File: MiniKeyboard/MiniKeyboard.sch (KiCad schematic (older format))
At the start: 50 parts

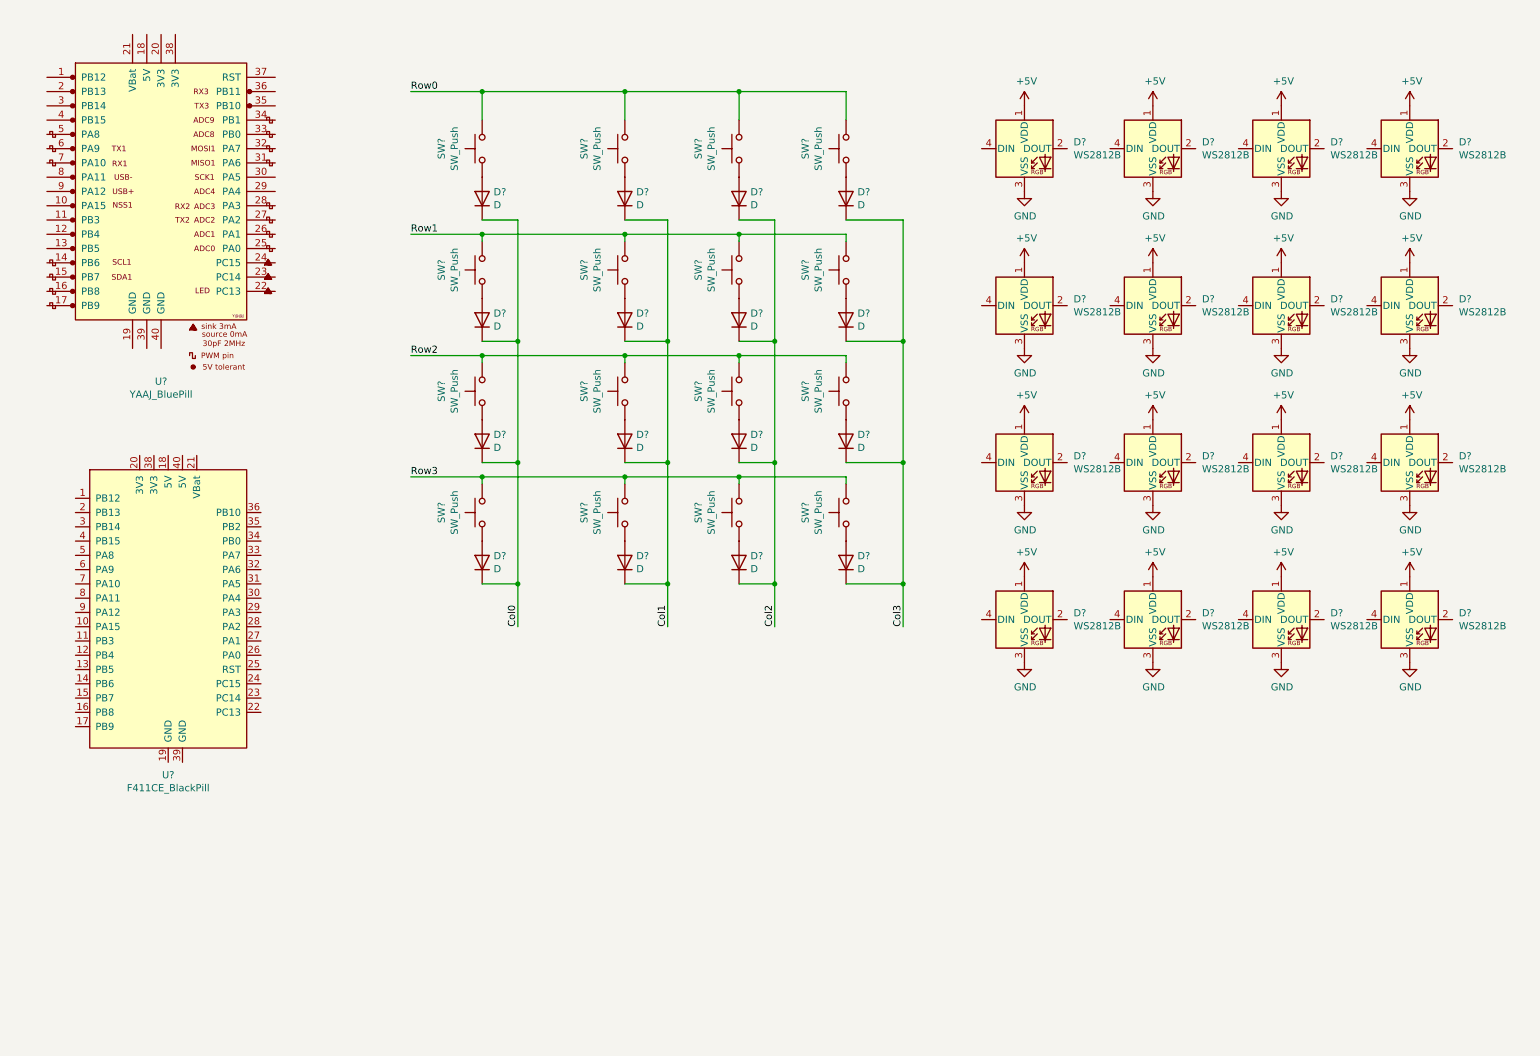
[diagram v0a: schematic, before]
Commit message: Added 411CE Blackpill to minikeyboard
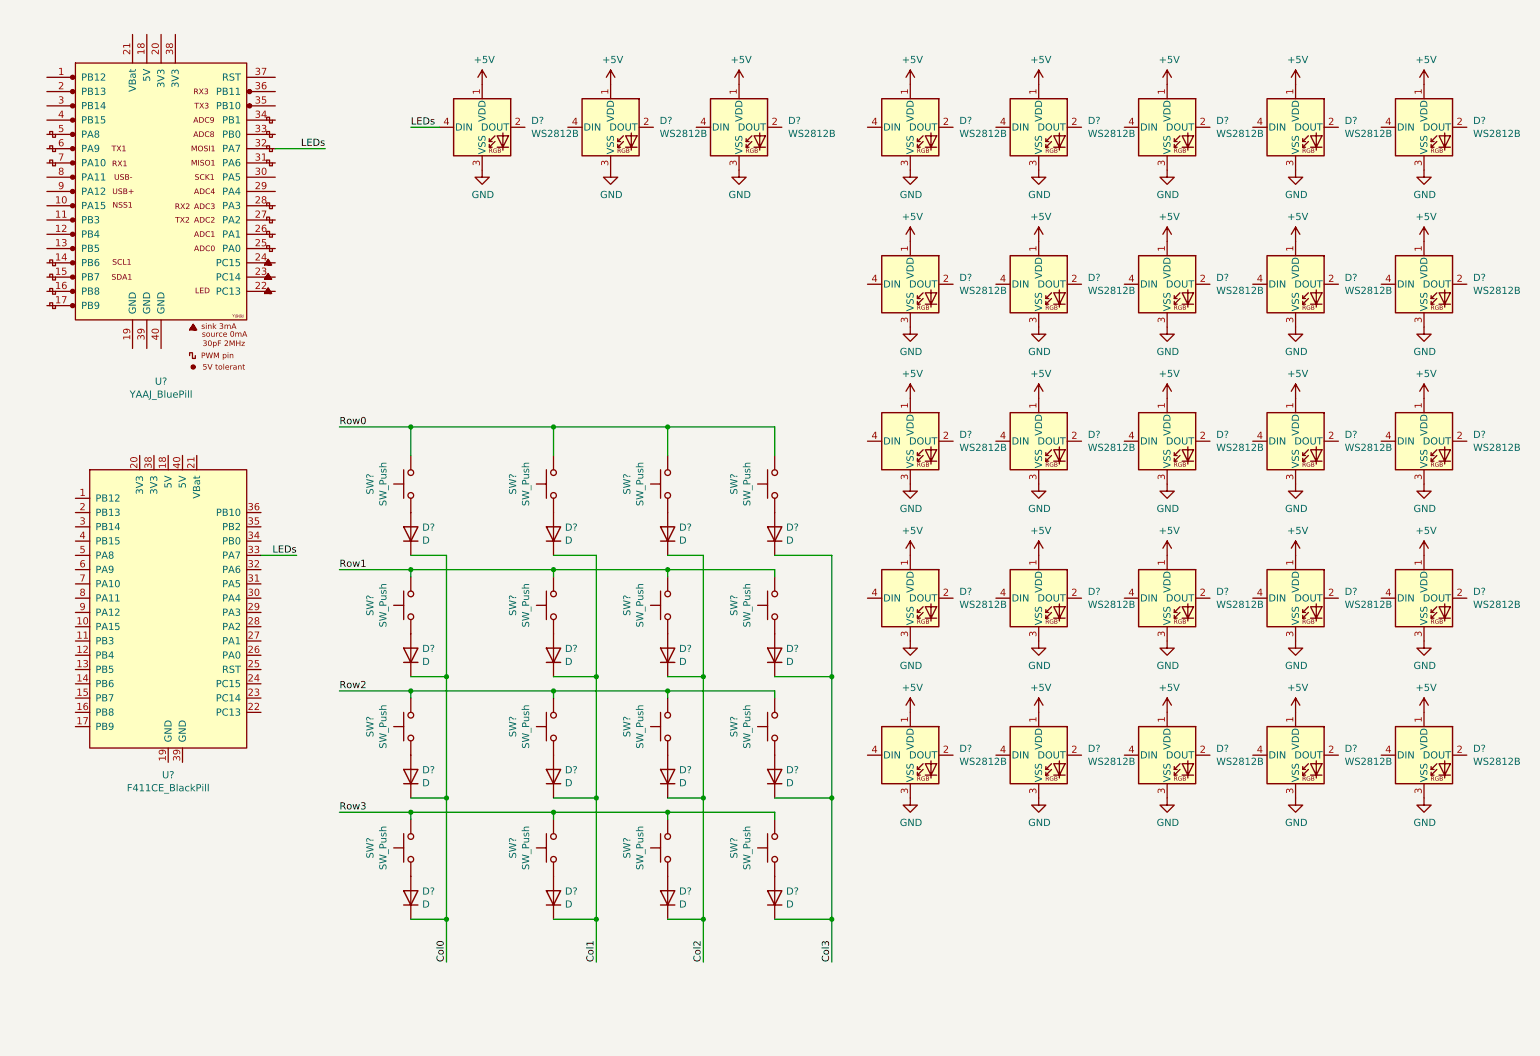
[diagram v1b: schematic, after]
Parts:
- added D? (x12): WS2812B, LED_SMD:LED_WS2812B_PLCC4_5.0x5.0mm_P3.2mm, symbol LED:WS2812B
- U?: footprint (none) -> MiniKeyboard:F411CE-Blackpill
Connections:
- net +5V: now also D?.1 (VDD), D?.1 (VDD), D?.1 (VDD), D?.1 (VDD), D?.1 (VDD), D?.1 (VDD), D?.1 (VDD), D?.1 (VDD), D?.1 (VDD), D?.1 (VDD), D?.1 (VDD), D?.1 (VDD)
- net GND: now also D?.3 (VSS), D?.3 (VSS), D?.3 (VSS), D?.3 (VSS), D?.3 (VSS), D?.3 (VSS), D?.3 (VSS), D?.3 (VSS), D?.3 (VSS), D?.3 (VSS), D?.3 (VSS), D?.3 (VSS)
- net LEDs: now reaches U?.33 (PA7)
- net LEDs: now also U?.32 (PA7), D?.4 (DIN)
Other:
- moved on the sheet: D?, SW?

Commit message: fixed minikeyboard after moving libraries around
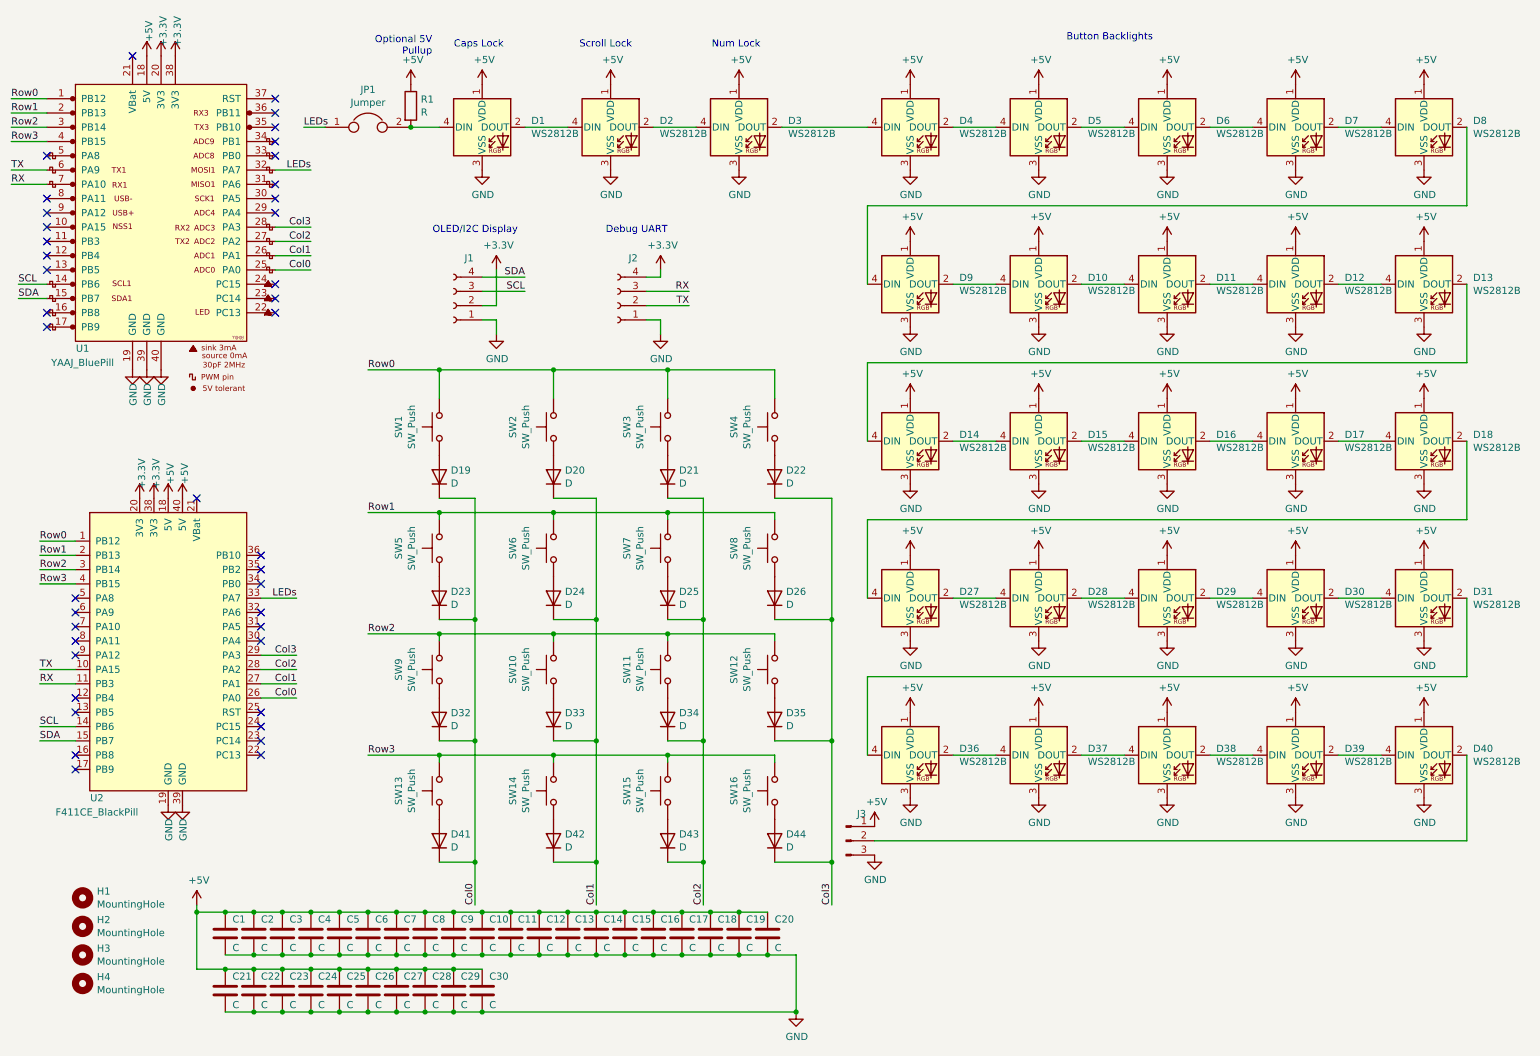
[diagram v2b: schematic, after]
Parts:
- added C1, C10, C11, C12, C13, C14, C15, C16, C17, C18, C19, C2, C20, C21, C22, C23, C24, C25, C26, C27, C28, C29, C3, C30, C4, C5, C6, C7, C8, C9: C, Capacitor_SMD:C_0805_2012Metric_Pad1.18x1.45mm_HandSolder, symbol Device:C
- added H1, H2, H3, H4: MountingHole, MountingHole:MountingHole_5mm, symbol Mechanical:MountingHole
- added J1, J2: Conn_01x04_Female, Connector_PinSocket_2.54mm:PinSocket_1x04_P2.54mm_Vertical, symbol Connector:Conn_01x04_Female
- added J3: Conn_01x03_Male, Connector_PinSocket_2.54mm:PinSocket_1x03_P2.54mm_Vertical, symbol Connector:Conn_01x03_Male
- added JP1: Jumper, Jumper:SolderJumper-2_P1.3mm_Bridged_RoundedPad1.0x1.5mm, symbol Device:Jumper
- added R1: R, Resistor_SMD:R_1206_3216Metric_Pad1.30x1.75mm_HandSolder, symbol Device:R
- D19, D20, D21, D22, D23, D24, D25, D26, D32, D33, D34, D35, D41, D42, D43, D44: renamed from D?; footprint (none) -> Diode_SMD:D_0805_2012Metric_Pad1.15x1.40mm_HandSolder
- SW1, SW10, SW11, SW12, SW13, SW14, SW15, SW16, SW2, SW3, SW4, SW5, SW6, SW7, SW8, SW9: renamed from SW?; footprint (none) -> Button_Switch_Keyboard:SW_Cherry_MX_1.00u_PCB
- gave numbers to parts that had none: 30
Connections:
- net +5V: now also U1.18 (5V), U2.18 (5V), U2.40 (5V), C1.1, C10.1, C11.1, C12.1, C13.1, C14.1, C15.1, C16.1, C17.1, C18.1, C19.1, C2.1, C20.1, C21.1, C22.1, C23.1, C24.1, C25.1, C26.1, C27.1, C28.1, C29.1, C3.1, C30.1, C4.1, C5.1, C6.1, C7.1, C8.1, C9.1, J3.1 (Pin_1), R1.1
- net Col0: now also U1.25 (PA0), U2.26 (PA0)
- net Col1: now also U1.26 (PA1), U2.27 (PA1)
- net Col2: now also U1.27 (PA2), U2.28 (PA2)
- net Col3: now also U1.28 (PA3), U2.29 (PA3)
- net GND: now also U1.19 (GND), U1.39 (GND), U1.40 (GND), U2.19 (GND), U2.39 (GND), C1.2, C10.2, C11.2, C12.2, C13.2, C14.2, C15.2, C16.2, C17.2, C18.2, C19.2, C2.2, C20.2, C21.2, C22.2, C23.2, C24.2, C25.2, C26.2, C27.2, C28.2, C29.2, C3.2, C30.2, C4.2, C5.2, C6.2, C7.2, C8.2, C9.2, J1.1 (Pin_1), J2.1 (Pin_1), J3.3 (Pin_3)
- net LEDs: now also JP1.1; no longer D1.4 (DIN)
- net Row0: now also U1.1 (PB12), U2.1 (PB12)
- net Row1: now also U1.2 (PB13), U2.2 (PB13)
- net Row2: now also U1.3 (PB14), U2.3 (PB14)
- net Row3: now also U1.4 (PB15), U2.4 (PB15)
- net TX: now reaches U2.10 (PA15)
- net TX: now also U1.6 (PA9), J2.2 (Pin_2)
- net RX: now reaches U2.11 (PB3)
- net RX: now also U1.7 (PA10), J2.3 (Pin_3)
- net SCL: now reaches U2.14 (PB6)
- net SCL: now also U1.14 (PB6), J1.3 (Pin_3)
- net SDA: now reaches U2.15 (PB7)
- net SDA: now also U1.15 (PB7), J1.4 (Pin_4)
- net +3V3: now reaches U2.20 (3V3)
- net +3V3: now also U1.20 (3V3), U1.38 (3V3), U2.38 (3V3), J1.2 (Pin_2), J2.4 (Pin_4)
- net at D10.2 (DOUT): now also D11.4 (DIN)
- net at D10.4 (DIN): now also D9.2 (DOUT)
- net at D11.2 (DOUT): now also D12.4 (DIN)
- net at D12.2 (DOUT): now also D13.4 (DIN)
- net at D13.2 (DOUT): now also D14.4 (DIN)
- net at D15.2 (DOUT): now also D16.4 (DIN)
- net at D15.4 (DIN): now also D14.2 (DOUT)
- net at D16.2 (DOUT): now also D17.4 (DIN)
- net at D17.2 (DOUT): now also D18.4 (DIN)
- net at D18.2 (DOUT): now also D27.4 (DIN)
- net at D28.2 (DOUT): now also D29.4 (DIN)
- net at D28.4 (DIN): now also D27.2 (DOUT)
- net at D29.2 (DOUT): now also D30.4 (DIN)
- net at D30.2 (DOUT): now also D31.4 (DIN)
- net at D31.2 (DOUT): now also D36.4 (DIN)
- net at D37.2 (DOUT): now also D38.4 (DIN)
- net at D37.4 (DIN): now also D36.2 (DOUT)
- net at D38.2 (DOUT): now also D39.4 (DIN)
- net at D39.2 (DOUT): now also D40.4 (DIN)
- net at D40.2 (DOUT): now also J3.2 (Pin_2)
- net at D9.4 (DIN): now also D8.2 (DOUT)
- net at D5.2 (DOUT): now also D6.4 (DIN)
- net at D5.4 (DIN): now also D4.2 (DOUT)
- net at D6.2 (DOUT): now also D7.4 (DIN)
- net at D7.2 (DOUT): now also D8.4 (DIN)
- net at D4.4 (DIN): now also D3.2 (DOUT)
- net at D2.2 (DOUT): now also D3.4 (DIN)
- net at D2.4 (DIN): now also D1.2 (DOUT)
- new net: D1.4 (DIN), JP1.2, R1.2
- no-connect marks 0 -> 41
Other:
- note added: "Button Backlights"
- note added: "Caps Lock"
- note added: "Debug UART"
- note added: "Num Lock"
- note added: "OLED/I2C Display"
- note added: "Optional 5V\nPullup"
- note added: "Scroll Lock"
- moved on the sheet: D19, D20, D21, D22, D23, D24, D25, D26, D32, D33, D34, D35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

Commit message: mini keyboard layout
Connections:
- net +3V3: now also C29.1, C30.1
- net +5V: no longer C29.1, C30.1
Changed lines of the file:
@@
 Wire Wire Line
 	3300 7250 3100 7250
-Connection ~ 3500 7250
 Wire Wire Line
 	3500 7250 3300 7250
-Connection ~ 3700 7250
-Wire Wire Line
-	3700 7250 3500 7250
 Wire Wire Line
 	1900 6850 2100 6850
@@
 NoConn ~ 1050 4750
 NoConn ~ 1050 4850
+$Comp
+L power:+3V3 #PWR?
+U 1 1 6090BA37
+P 4100 7250
+F 0 "#PWR?" H 4100 7100 50  0001 C CNN
+F 1 "+3V3" V 4115 7378 50  0000 L CNN
+F 2 "" H 4100 7250 50  0001 C CNN
+F 3 "" H 4100 7250 50  0001 C CNN
+	1    4100 7250
+	0    1    1    0
+$EndComp
+Wire Wire Line
+	4100 7250 3900 7250
+Connection ~ 3900 7250
 $EndSCHEMATC

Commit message: changed minikeyboard diodes and generated gerbers
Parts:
- D19, D20, D21, D22, D23, D24, D25, D26, D32, D33, D34, D35, D41, D42, D43, D44: footprint Diode_SMD:D_0805_2012Metric_Pad1.15x1.40mm_HandSolder -> Diode_SMD:D_SOT-23_ANK
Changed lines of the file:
@@
 F 0 "D19" V 3646 3720 50  0000 R CNN
 F 1 "D" V 3555 3720 50  0000 R CNN
-F 2 "Diode_SMD:D_0805_2012Metric_Pad1.15x1.40mm_HandSolder" H 3600 3800 50  0001 C CNN
+F 2 "Diode_SMD:D_SOT-23_ANK" H 3600 3800 50  0001 C CNN
 F 3 "~" H 3600 3800 50  0001 C CNN
 	1    3600 3800
@@
 F 0 "D23" V 3646 4570 50  0000 R CNN
 F 1 "D" V 3555 4570 50  0000 R CNN
-F 2 "Diode_SMD:D_0805_2012Metric_Pad1.15x1.40mm_HandSolder" H 3600 4650 50  0001 C CNN
+F 2 "Diode_SMD:D_SOT-23_ANK" H 3600 4650 50  0001 C CNN
 F 3 "~" H 3600 4650 50  0001 C CNN
 	1    3600 4650
@@
 F 0 "D32" V 3646 5420 50  0000 R CNN
 F 1 "D" V 3555 5420 50  0000 R CNN
-F 2 "Diode_SMD:D_0805_2012Metric_Pad1.15x1.40mm_HandSolder" H 3600 5500 50  0001 C CNN
+F 2 "Diode_SMD:D_SOT-23_ANK" H 3600 5500 50  0001 C CNN
 F 3 "~" H 3600 5500 50  0001 C CNN
 	1    3600 5500
@@
 F 0 "D41" V 3646 6270 50  0000 R CNN
 F 1 "D" V 3555 6270 50  0000 R CNN
-F 2 "Diode_SMD:D_0805_2012Metric_Pad1.15x1.40mm_HandSolder" H 3600 6350 50  0001 C CNN
+F 2 "Diode_SMD:D_SOT-23_ANK" H 3600 6350 50  0001 C CNN
 F 3 "~" H 3600 6350 50  0001 C CNN
 	1    3600 6350
@@
 F 0 "D20" V 4446 3720 50  0000 R CNN
 F 1 "D" V 4355 3720 50  0000 R CNN
-F 2 "Diode_SMD:D_0805_2012Metric_Pad1.15x1.40mm_HandSolder" H 4400 3800 50  0001 C CNN
+F 2 "Diode_SMD:D_SOT-23_ANK" H 4400 3800 50  0001 C CNN
 F 3 "~" H 4400 3800 50  0001 C CNN
 	1    4400 3800
@@
 F 0 "D24" V 4446 4570 50  0000 R CNN
 F 1 "D" V 4355 4570 50  0000 R CNN
-F 2 "Diode_SMD:D_0805_2012Metric_Pad1.15x1.40mm_HandSolder" H 4400 4650 50  0001 C CNN
+F 2 "Diode_SMD:D_SOT-23_ANK" H 4400 4650 50  0001 C CNN
 F 3 "~" H 4400 4650 50  0001 C CNN
 	1    4400 4650
@@
 F 0 "D33" V 4446 5420 50  0000 R CNN
 F 1 "D" V 4355 5420 50  0000 R CNN
-F 2 "Diode_SMD:D_0805_2012Metric_Pad1.15x1.40mm_HandSolder" H 4400 5500 50  0001 C CNN
+F 2 "Diode_SMD:D_SOT-23_ANK" H 4400 5500 50  0001 C CNN
 F 3 "~" H 4400 5500 50  0001 C CNN
 	1    4400 5500
@@
 F 0 "D42" V 4446 6270 50  0000 R CNN
 F 1 "D" V 4355 6270 50  0000 R CNN
-F 2 "Diode_SMD:D_0805_2012Metric_Pad1.15x1.40mm_HandSolder" H 4400 6350 50  0001 C CNN
+F 2 "Diode_SMD:D_SOT-23_ANK" H 4400 6350 50  0001 C CNN
 F 3 "~" H 4400 6350 50  0001 C CNN
 	1    4400 6350
@@
 F 0 "D21" V 5246 3720 50  0000 R CNN
 F 1 "D" V 5155 3720 50  0000 R CNN
-F 2 "Diode_SMD:D_0805_2012Metric_Pad1.15x1.40mm_HandSolder" H 5200 3800 50  0001 C CNN
+F 2 "Diode_SMD:D_SOT-23_ANK" H 5200 3800 50  0001 C CNN
 F 3 "~" H 5200 3800 50  0001 C CNN
 	1    5200 3800
@@
 F 0 "D25" V 5246 4570 50  0000 R CNN
 F 1 "D" V 5155 4570 50  0000 R CNN
-F 2 "Diode_SMD:D_0805_2012Metric_Pad1.15x1.40mm_HandSolder" H 5200 4650 50  0001 C CNN
+F 2 "Diode_SMD:D_SOT-23_ANK" H 5200 4650 50  0001 C CNN
 F 3 "~" H 5200 4650 50  0001 C CNN
 	1    5200 4650
@@
 F 0 "D34" V 5246 5420 50  0000 R CNN
 F 1 "D" V 5155 5420 50  0000 R CNN
-F 2 "Diode_SMD:D_0805_2012Metric_Pad1.15x1.40mm_HandSolder" H 5200 5500 50  0001 C CNN
+F 2 "Diode_SMD:D_SOT-23_ANK" H 5200 5500 50  0001 C CNN
 F 3 "~" H 5200 5500 50  0001 C CNN
 	1    5200 5500
@@
 F 0 "D43" V 5246 6270 50  0000 R CNN
 F 1 "D" V 5155 6270 50  0000 R CNN
-F 2 "Diode_SMD:D_0805_2012Metric_Pad1.15x1.40mm_HandSolder" H 5200 6350 50  0001 C CNN
+F 2 "Diode_SMD:D_SOT-23_ANK" H 5200 6350 50  0001 C CNN
 F 3 "~" H 5200 6350 50  0001 C CNN
 	1    5200 6350
@@
 F 0 "D22" V 5996 3720 50  0000 R CNN
 F 1 "D" V 5905 3720 50  0000 R CNN
-F 2 "Diode_SMD:D_0805_2012Metric_Pad1.15x1.40mm_HandSolder" H 5950 3800 50  0001 C CNN
+F 2 "Diode_SMD:D_SOT-23_ANK" H 5950 3800 50  0001 C CNN
 F 3 "~" H 5950 3800 50  0001 C CNN
 	1    5950 3800
@@
 F 0 "D26" V 5996 4570 50  0000 R CNN
 F 1 "D" V 5905 4570 50  0000 R CNN
-F 2 "Diode_SMD:D_0805_2012Metric_Pad1.15x1.40mm_HandSolder" H 5950 4650 50  0001 C CNN
+F 2 "Diode_SMD:D_SOT-23_ANK" H 5950 4650 50  0001 C CNN
 F 3 "~" H 5950 4650 50  0001 C CNN
 	1    5950 4650
@@
 F 0 "D35" V 5996 5420 50  0000 R CNN
 F 1 "D" V 5905 5420 50  0000 R CNN
-F 2 "Diode_SMD:D_0805_2012Metric_Pad1.15x1.40mm_HandSolder" H 5950 5500 50  0001 C CNN
+F 2 "Diode_SMD:D_SOT-23_ANK" H 5950 5500 50  0001 C CNN
 F 3 "~" H 5950 5500 50  0001 C CNN
 	1    5950 5500
@@
 F 0 "D44" V 5996 6270 50  0000 R CNN
 F 1 "D" V 5905 6270 50  0000 R CNN
-F 2 "Diode_SMD:D_0805_2012Metric_Pad1.15x1.40mm_HandSolder" H 5950 6350 50  0001 C CNN
+F 2 "Diode_SMD:D_SOT-23_ANK" H 5950 6350 50  0001 C CNN
 F 3 "~" H 5950 6350 50  0001 C CNN
 	1    5950 6350
